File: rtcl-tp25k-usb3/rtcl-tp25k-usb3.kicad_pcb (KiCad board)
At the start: 4 copper layers, 80 x 35 mm, 109 parts, among them J1 ZX360D-B-10P(30), J10 SSQ-106-02-F-D-RA, J2 CF20221V0R0-NH, J3 DF40C(2.0)-60DS-0.4V(51), J4 DF40C(2.0)-60DS-0.4V(51), J5 JTAG, J6 Conn_01x02, J7 Conn_01x03, Q2 NTK3134NT1G, Q3 NTK3134NT1G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

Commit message: WIP
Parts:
- RN1, RN2, RN3, RN4, RN5, RN6, RN7, RN8, RN9: footprint rtcl-tp25k-usb3:RES_YC104_YAG -> rtcl-tp25k-usb3:ARRAY_FR-072K2L_YAG
- moved RN2 1.36 mm to (124.3, 107.4)
- moved RN6 1.31 mm to (136.4, 103.7)
- moved C18 1.30 mm to (135.4, 105.4)
- moved C5 1.24 mm to (121.5, 106.3)
- moved RN5 1.22 mm to (134.0, 107.4)
- moved R43 1.21 mm to (136.0, 107.0), turned to -90 degrees
- moved RN9 1.04 mm to (136.4, 95.3)
- moved RN7 0.94 mm to (136.4, 101.2)
- moved RN3 0.89 mm to (126.9, 107.4)
- moved RN8 0.85 mm to (136.4, 97.8)
- moved RN4 0.76 mm to (131.4, 107.4)
- moved C16 0.20 mm to (135.6, 99.5)
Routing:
- net GND: track 278.1 -> 264.8 mm, vias 70 -> 68
- net /K5_IOT63B: track 14.1 -> 8.76 mm
- net Net-(U1-DV10): track 49.2 -> 46.4 mm
- net /H5_IOT61A: track 14.4 -> 12.6 mm
- net /FT601_D0: track 2.23 -> 3.87 mm
- net /J5_IOT61B: track 14.9 -> 13.4 mm
- net /L5_IOT63A: track 15.4 -> 13.8 mm
- net /FT601_D16: track 1.97 -> 3.44 mm
- net /L9_IOT31A_40P: track 15.2 -> 13.7 mm
- net /K9_IOT31B_40P: track 15.8 -> 14.4 mm
- net /J8_IOT56A_40P: track 16.1 -> 14.8 mm
- net /FT601_CLK: track 3.11 -> 4.45 mm
- net /K8_IOT56B_40P: track 16.4 -> 15.0 mm
- net /FT601_D18: track 1.97 -> 3.22 mm
- net /F7_IOT58A_40P: track 18.4 -> 17.1 mm
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
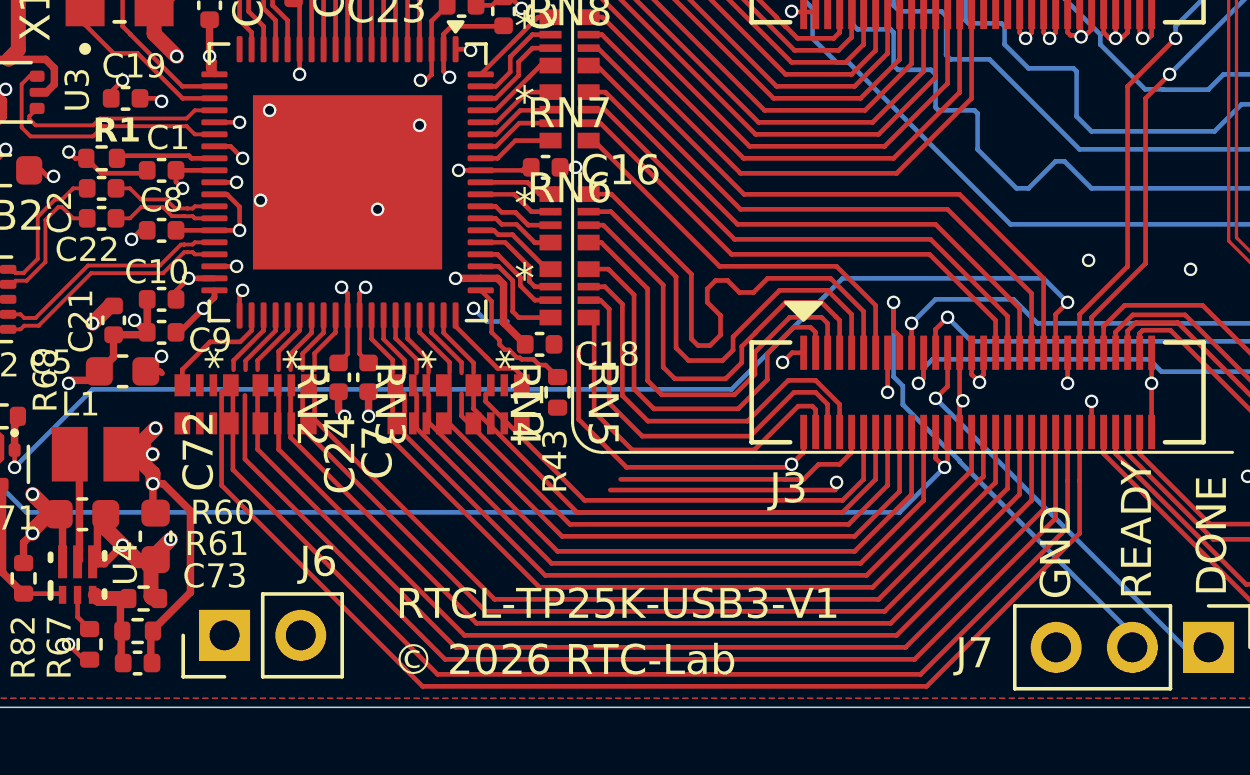
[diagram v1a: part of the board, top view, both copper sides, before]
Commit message: Update visible_layers in rtcl-tp25k-usb3.kicad_prl to correct layer visibility settings
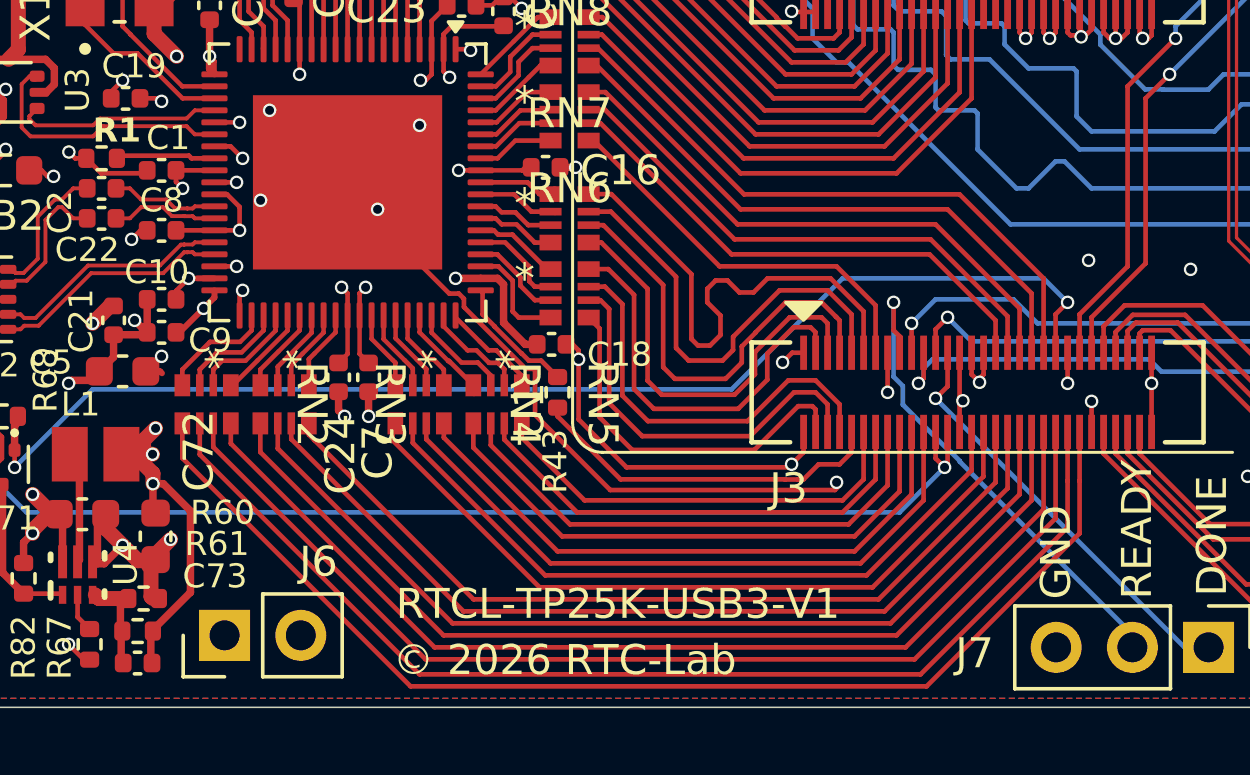
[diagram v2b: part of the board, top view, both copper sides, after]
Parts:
- moved C18 0.40 mm to (135.8, 105.4)
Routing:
- net GND: track 264.8 -> 278.2 mm
- net /K5_IOT63B: track 8.76 -> 12.0 mm
- net /H8_IOT66A: track 16.1 -> 14.6 mm
- net /FT601_D1: track 2.23 -> 3.69 mm
- net /H7_IOT66B: track 17.4 -> 16.0 mm
- net /FT601_D2: track 2.23 -> 3.65 mm
- net /G7_IOT68A: track 18.8 -> 17.4 mm
- net /G8_IOT68B: track 20.2 -> 18.8 mm
- net /F5_IOT72A: track 21.7 -> 20.5 mm
- net /FT601_D14: track 2.33 -> 3.52 mm
- net /FT601_D13: track 2.33 -> 3.46 mm
- net /L6_IOT23A_USB_P: track 24.9 -> 23.8 mm
- net /G5_IOT72B: track 23.1 -> 22.0 mm
- net /K6_IOT23B_USB_N: track 26.3 -> 25.3 mm
- net /FT601_D3: track 2.23 -> 3.15 mm
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
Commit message: WIP
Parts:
- moved R45 4.74 mm to (129.4, 93.6), turned to 90 degrees
- moved R44 2.43 mm to (130.3, 91.6), turned to 90 degrees
- moved RN1 1.35 mm to (133.6, 91.7)
- moved C25 0.98 mm to (133.3, 93.9)
- moved C23 0.54 mm to (132.3, 93.9), turned to -90 degrees
- moved RN6 0.50 mm to (135.9, 103.7)
- moved RN7 0.50 mm to (135.9, 101.2)
- moved RN9 0.48 mm to (135.9, 95.2)
- moved RN8 0.47 mm to (135.9, 97.8)
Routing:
- net /K4_IOR22B_40P: track 18.4 -> 24.8 mm
- net /FT601_RXF: track 6.81 -> 1.45 mm
- net /G2_IOR24A_40P: track 19.3 -> 22.4 mm
- net /FT601_TXE: track 5.82 -> 3.32 mm
- net Net-(U1-DV10): track 46.4 -> 48.7 mm
- net /FT601_BE0: track 2.86 -> 4.01 mm
- net /FT601_BE1: track 3.60 -> 4.74 mm
- net /FT601_BE2: track 4.34 -> 5.38 mm
- net /J1_IOR33A_40P: track 21.5 -> 20.6 mm
- net /L3_IOR31B_40P: track 20.9 -> 20.0 mm
- net /FT601_BE3: track 5.03 -> 5.88 mm
- net /L4_IOR31A_40P: track 20.2 -> 19.4 mm
- net Net-(U1-AVDD): track 22.1 -> 21.4 mm
- net /G1_IOR24B_40P: track 19.5 -> 18.7 mm
- net /FT601_SIWU: track 26.7 -> 27.4 mm
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
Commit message: WIP
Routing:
- net /L9_IOT31A_40P: track 13.7 -> 14.2 mm
- net /L5_IOT63A: track 13.8 -> 14.3 mm
- net /J5_IOT61B: track 13.4 -> 13.9 mm
- net /H5_IOT61A: track 12.5 -> 13.0 mm

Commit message: WIP
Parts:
- moved C23 0.14 mm to (132.4, 93.8)
- moved C25 0.14 mm to (133.4, 93.8)
- moved RN1 0.10 mm to (133.6, 91.6)

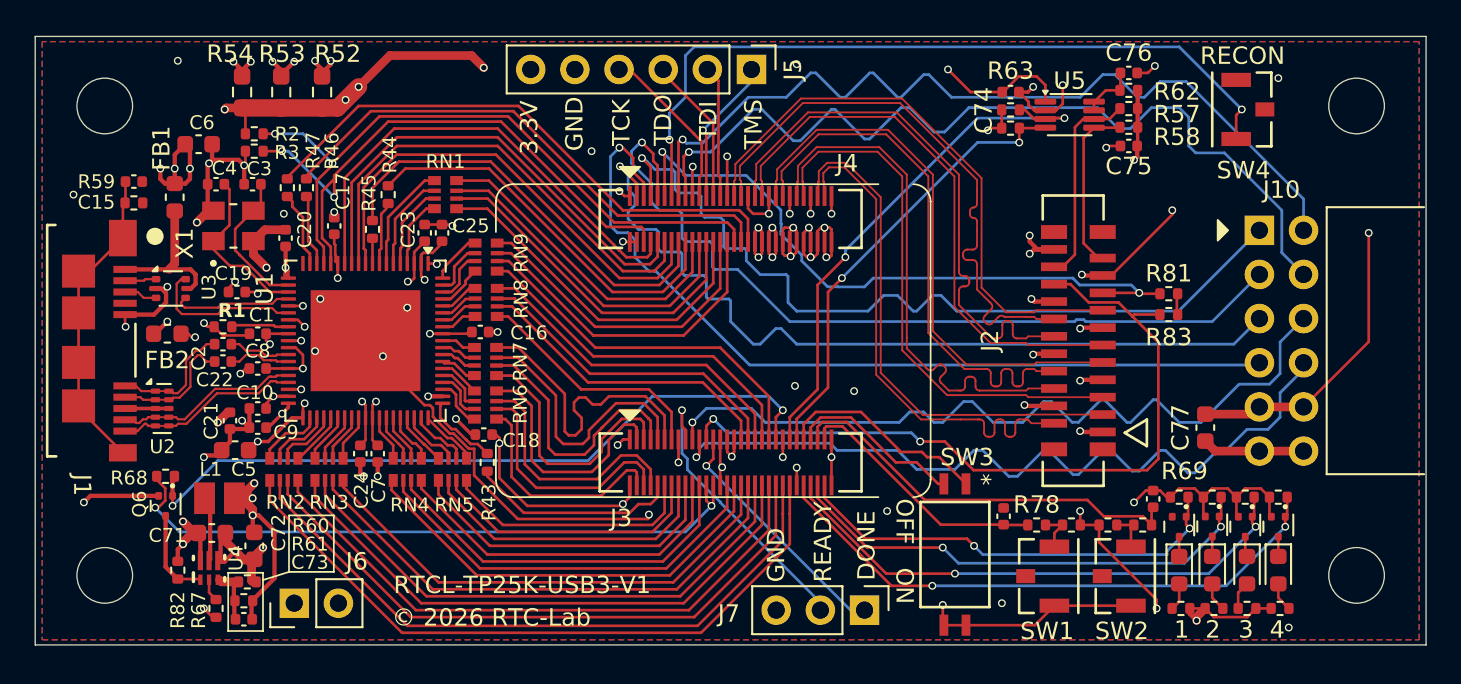
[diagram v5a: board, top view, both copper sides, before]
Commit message: Fix visibility settings in KiCad project file for improved layer management
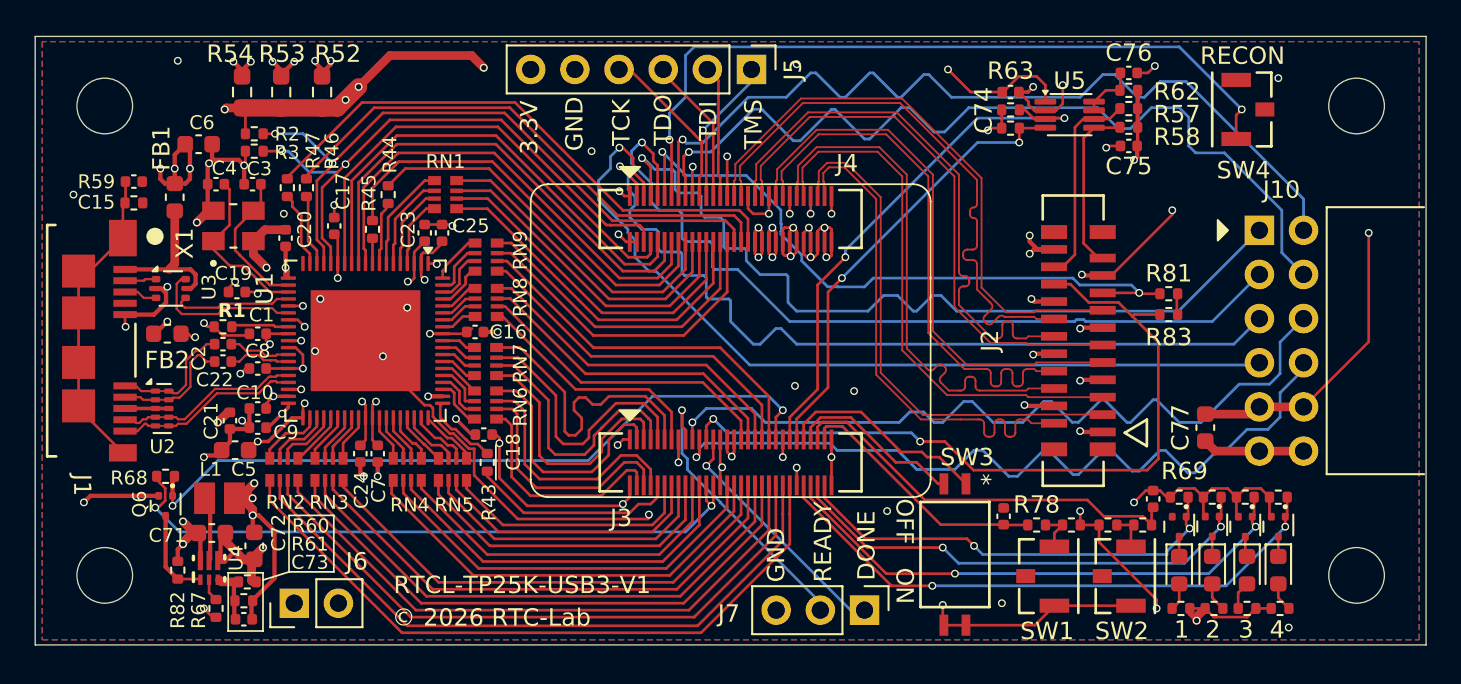
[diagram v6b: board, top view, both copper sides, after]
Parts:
- moved C16 0.30 mm to (135.3, 99.5)
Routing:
- net /FT601_RESET: track 34.4 -> 32.8 mm

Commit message: Update active layer and visible layers in KiCad project file
- Changed active layer from 0 to 4 for improved design visibility.
- Updated visible layers from "00000000_00000000_00000080_82082027" to "00000000_00000000_00000080_82082077" to reflect new layer settings.
- Modified zone display mode from 1 to 0 for better layout management.
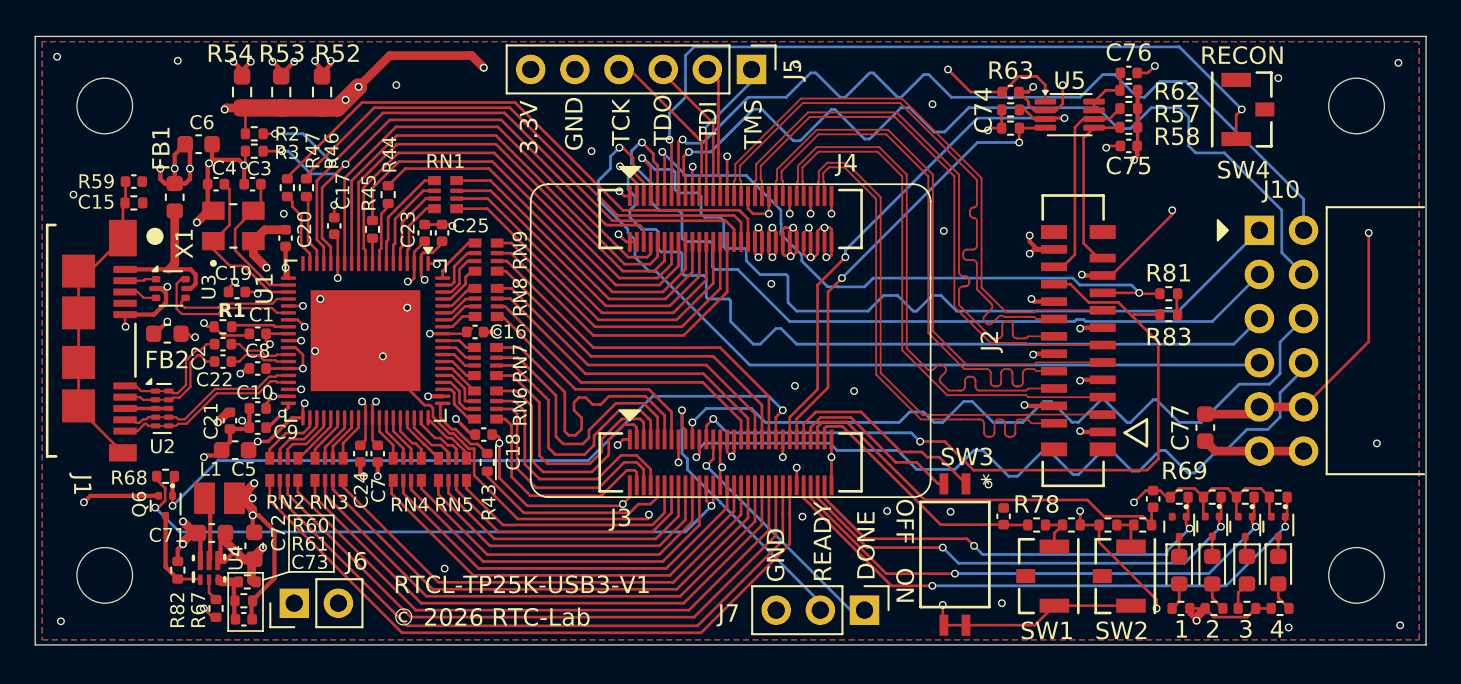
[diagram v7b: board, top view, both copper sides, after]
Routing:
- net GND: track 278.9 -> 371.6 mm, vias 68 -> 81
- net /FT601_RESET: track 32.8 -> 33.5 mm
- net +3V3: track 258.0 -> 258.6 mm

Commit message: WIP
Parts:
- moved C21 5.00 mm to (122.9, 99.9), turned to 0 degrees
- moved C8 0.84 mm to (122.4, 98.9)
- moved R1 0.37 mm to (120.4, 99.2)
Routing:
- net GND: track 371.6 -> 379.2 mm, vias 81 -> 83
- net Net-(U1-RREF): track 3.33 -> 6.03 mm, vias 0 -> 2
- net Net-(U1-DV10): track 48.7 -> 46.4 mm, vias 7 -> 6
- net +3V3: track 258.6 -> 258.0 mm
